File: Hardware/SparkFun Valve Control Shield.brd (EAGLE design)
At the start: 55.9 x 73.7 mm, 112 parts, among them J1 5.5x2.1mm Barrel, Q3 100A/100V/6.8mΩ, Q4 100A/100V/6.8mΩ, SW2 Start

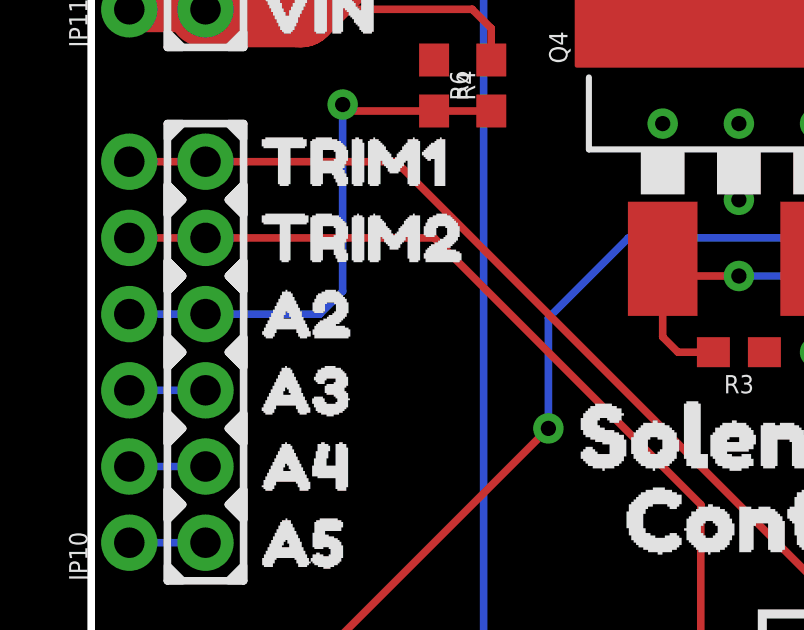
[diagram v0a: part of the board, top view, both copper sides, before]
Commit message: Add readme, udpate silk on vin, and add ignore.
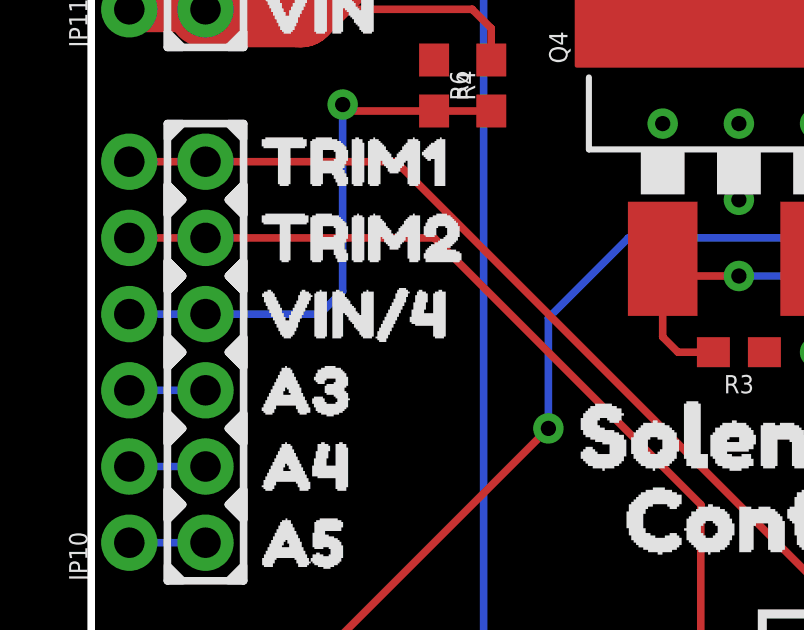
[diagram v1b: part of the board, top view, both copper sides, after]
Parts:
- added U$80: (no value), buzzard_labels (2):VIN#40
- U$27: device buzzard_labels (17):A21 -> buzzard_labels (2):VIN#40
- U$56: device buzzard_labels (17):A21 -> OSHW_mark_US000262#png (1):OSHW_MARK_US000262#PNG
- moved U$56 21.2 mm to (27.9, 15.2)
- moved U$27 8.89 mm to (13.2, 26.7), flipped to the bottom
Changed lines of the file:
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@@
 <element name="U$24" library="buzzard_labels (17)" package="3#3V8" value="" x="4.318" y="46.99" smashed="yes"/>
 <element name="U$25" library="buzzard_labels (17)" package="5V7" value="" x="4.318" y="44.45" smashed="yes"/>
-<element name="U$27" library="buzzard_labels (17)" package="A21" value="" x="4.318" y="26.67" smashed="yes"/>
 <element name="U$28" library="buzzard_labels (17)" package="A32" value="" x="4.064" y="24.13" smashed="yes"/>
 <element name="U$29" library="buzzard_labels (17)" package="A43" value="" x="4.064" y="21.59" smashed="yes"/>
@@
 <element name="U$54" library="buzzard_labels (17)" package="RESET9" value="" x="14.097" y="49.53" smashed="yes" rot="MR0"/>
 <element name="U$55" library="buzzard_labels" package="VIN0" value="" x="10.795" y="36.83" smashed="yes" rot="MR0"/>
-<element name="U$56" library="buzzard_labels (17)" package="A21" value="" x="10.033" y="26.67" smashed="yes" rot="MR0"/>
 <element name="U$57" library="buzzard_labels (17)" package="A32" value="" x="10.287" y="24.13" smashed="yes" rot="MR0"/>
 <element name="U$58" library="buzzard_labels (17)" package="A43" value="" x="10.287" y="21.59" smashed="yes" rot="MR0"/>
@@
 <element name="U$78" library="buzzard_labels (16)" package="215" value="" x="51.435" y="24.13" smashed="yes" rot="MR0"/>
 <element name="U$79" library="buzzard_labels (5)" package="BTN1" value="" x="51.435" y="36.83" smashed="yes" rot="MR0"/>
+<element name="U$80" library="buzzard_labels (2)" package="VIN#40" value="" x="4.318" y="26.67" smashed="yes"/>
+<element name="U$27" library="buzzard_labels (2)" package="VIN#40" value="" x="13.208" y="26.67" smashed="yes" rot="MR0"/>
+<element name="U$56" library="OSHW_mark_US000262#png (1)" package="OSHW_MARK_US000262#PNG" value="" x="27.94" y="15.24" smashed="yes" rot="MR0"/>
 </elements>
 <signals>
